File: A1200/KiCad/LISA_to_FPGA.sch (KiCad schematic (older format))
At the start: 30 parts, among them J1 Conn_01x01, J2 Conn_01x40, U1 LM1117-3.3, U2 74LVC162244ADGG, U3 74LVC162244ADGG, U4 LISA, U5 RP2354B

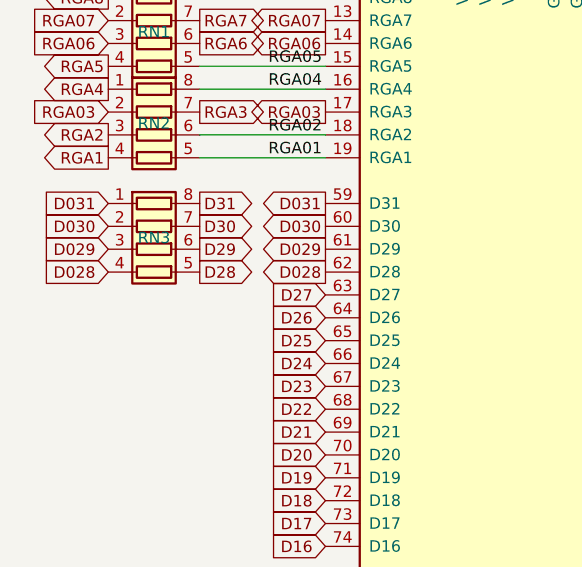
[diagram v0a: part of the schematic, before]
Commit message: Add RN4 resistor pack and route D27-D24
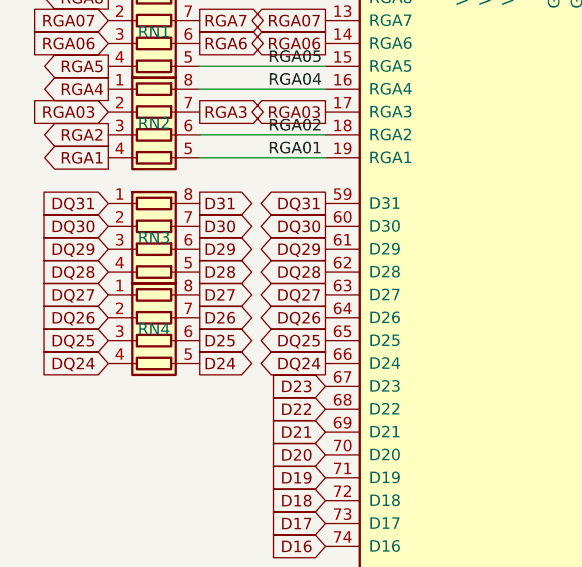
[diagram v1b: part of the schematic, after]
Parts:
- added RN4: R_Pack04, Resistor_SMD:R_Array_Convex_4x0603, symbol Device:R_Pack04
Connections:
- net D24: now also RN4.5 (R4.2); no longer U4.66 (D24)
- net D25: now also RN4.6 (R3.2); no longer U4.65 (D25)
- net D26: now also RN4.7 (R2.2); no longer U4.64 (D26)
- net D27: now also RN4.8 (R1.2); no longer U4.63 (D27)
- net D028 renamed DQ28
- net D029 renamed DQ29
- net D030 renamed DQ30
- net D031 renamed DQ31
- new net DQ24: RN4.4 (R4.1), U4.66 (D24)
- new net DQ25: RN4.3 (R3.1), U4.65 (D25)
- new net DQ26: RN4.2 (R2.1), U4.64 (D26)
- new net DQ27: RN4.1 (R1.1), U4.63 (D27)
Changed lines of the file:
@@
 Text GLabel 1150 2550 2    50   Output ~ 0
 D28
-Text GLabel 1700 2650 0    50   Input ~ 0
-D27
-Text GLabel 1700 2750 0    50   Input ~ 0
-D26
-Text GLabel 1700 2850 0    50   Input ~ 0
-D25
-Text GLabel 1700 2950 0    50   Input ~ 0
-D24
+Text GLabel 1700 2750 0    50   Output ~ 0
+DQ26
+Text GLabel 1700 2850 0    50   Output ~ 0
+DQ25
+Text GLabel 1700 2950 0    50   Output ~ 0
+DQ24
 Text GLabel 1700 3050 0    50   Input ~ 0
 D23
@@
 	1700 2050 1150 2050
 Text GLabel 1700 2250 0    50   Output ~ 0
-D031
+DQ31
 Text GLabel 1700 2350 0    50   Output ~ 0
-D030
+DQ30
 Text GLabel 1700 2450 0    50   Output ~ 0
-D029
+DQ29
 Text GLabel 1700 2550 0    50   Output ~ 0
-D028
+DQ28
 Text GLabel 750  2250 0    50   Input ~ 0
-D031
+DQ31
 Text GLabel 750  2350 0    50   Input ~ 0
-D030
+DQ30
 Text GLabel 750  2450 0    50   Input ~ 0
-D029
+DQ29
 Text GLabel 750  2550 0    50   Input ~ 0
-D028
+DQ28
+$Comp
+L Device:R_Pack04 RN4
+U 1 1 6AE6E351
+P 950 2850
+F 0 "RN4" V 900 2850 50  0000 C CNN
+F 1 "R_Pack04" V 950 2200 50  0001 C CNN
+F 2 "Resistor_SMD:R_Array_Convex_4x0603" V 1225 2850 50  0001 C CNN
+F 3 "~" H 950 2850 50  0001 C CNN
+	1    950  2850
+	0    1    1    0
+$EndComp
+Text GLabel 1700 2650 0    50   Output ~ 0
+DQ27
+Text GLabel 1150 2750 2    50   Output ~ 0
+D26
+Text GLabel 1150 2850 2    50   Output ~ 0
+D25
+Text GLabel 1150 2950 2    50   Output ~ 0
+D24
+Text GLabel 1150 2650 2    50   Output ~ 0
+D27
+Text GLabel 750  2650 0    50   Input ~ 0
+DQ27
+Text GLabel 750  2750 0    50   Input ~ 0
+DQ26
+Text GLabel 750  2850 0    50   Input ~ 0
+DQ25
+Text GLabel 750  2950 0    50   Input ~ 0
+DQ24
 $EndSCHEMATC

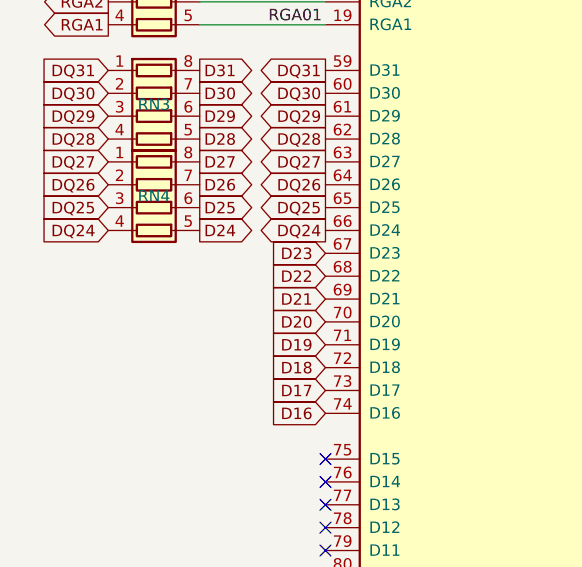
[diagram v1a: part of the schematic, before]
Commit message: Add RN5 resistor pack and route D23-D20
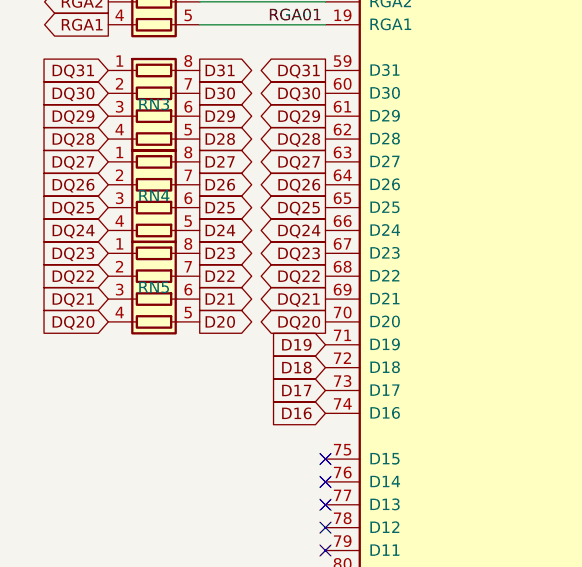
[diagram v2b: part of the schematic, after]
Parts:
- added RN5: R_Pack04, Resistor_SMD:R_Array_Convex_4x0603, symbol Device:R_Pack04
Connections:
- net D20: now also RN5.5 (R4.2); no longer U4.70 (D20)
- net D21: now also RN5.6 (R3.2); no longer U4.69 (D21)
- net D22: now also RN5.7 (R2.2); no longer U4.68 (D22)
- net D23: now also RN5.8 (R1.2); no longer U4.67 (D23)
- new net DQ20: RN5.4 (R4.1), U4.70 (D20)
- new net DQ21: RN5.3 (R3.1), U4.69 (D21)
- new net DQ22: RN5.2 (R2.1), U4.68 (D22)
- new net DQ23: RN5.1 (R1.1), U4.67 (D23)
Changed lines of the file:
@@
 Text GLabel 1700 2950 0    50   Output ~ 0
 DQ24
-Text GLabel 1700 3050 0    50   Input ~ 0
-D23
-Text GLabel 1700 3150 0    50   Input ~ 0
-D22
-Text GLabel 1700 3250 0    50   Input ~ 0
-D21
-Text GLabel 1700 3350 0    50   Input ~ 0
-D20
+Text GLabel 1700 3050 0    50   Output ~ 0
+DQ23
+Text GLabel 1700 3150 0    50   Output ~ 0
+DQ22
+Text GLabel 1700 3250 0    50   Output ~ 0
+DQ21
+Text GLabel 1700 3350 0    50   Output ~ 0
+DQ20
 Text GLabel 1700 3450 0    50   Input ~ 0
 D19
@@
 Text GLabel 750  2950 0    50   Input ~ 0
 DQ24
+$Comp
+L Device:R_Pack04 RN5
+U 1 1 6AEC9853
+P 950 3250
+F 0 "RN5" V 900 3250 50  0000 C CNN
+F 1 "R_Pack04" V 950 2600 50  0001 C CNN
+F 2 "Resistor_SMD:R_Array_Convex_4x0603" V 1225 3250 50  0001 C CNN
+F 3 "~" H 950 3250 50  0001 C CNN
+	1    950  3250
+	0    1    1    0
+$EndComp
+Text GLabel 750  3050 0    50   Input ~ 0
+DQ23
+Text GLabel 750  3150 0    50   Input ~ 0
+DQ22
+Text GLabel 750  3250 0    50   Input ~ 0
+DQ21
+Text GLabel 750  3350 0    50   Input ~ 0
+DQ20
+Text GLabel 1150 3050 2    50   Output ~ 0
+D23
+Text GLabel 1150 3150 2    50   Output ~ 0
+D22
+Text GLabel 1150 3250 2    50   Output ~ 0
+D21
+Text GLabel 1150 3350 2    50   Output ~ 0
+D20
 $EndSCHEMATC

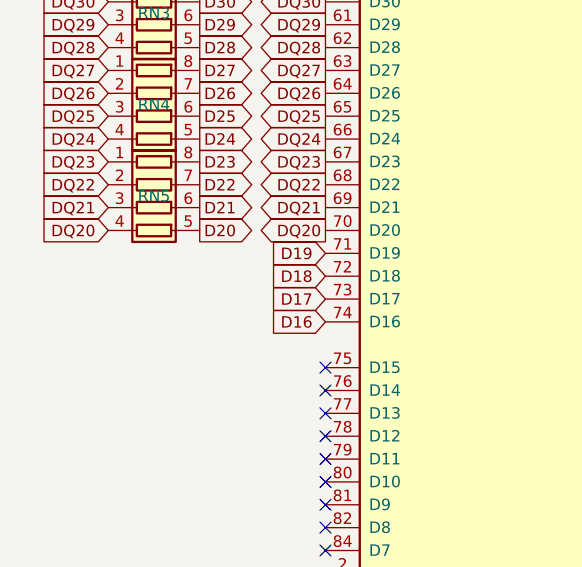
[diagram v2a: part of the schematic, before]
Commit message: Add RN6 resistor pack and route D19-D16, and some silkscreen fixes
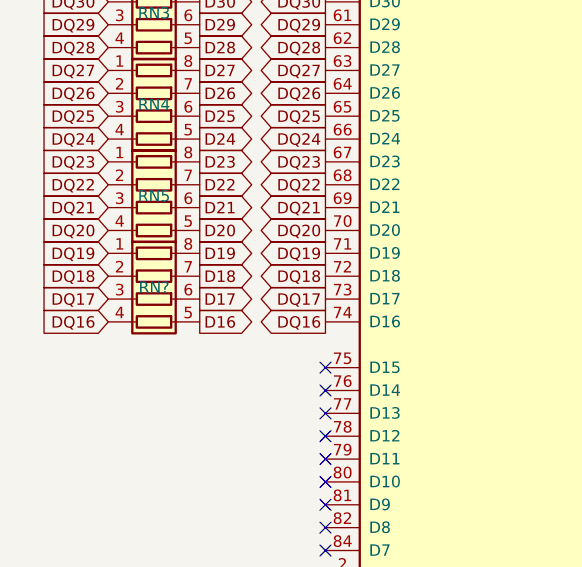
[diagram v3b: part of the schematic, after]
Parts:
- added RN?: R_Pack04, Resistor_SMD:R_Array_Convex_4x0603, symbol Device:R_Pack04
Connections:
- net D16: now also RN?.5 (R4.2); no longer U4.74 (D16)
- net D17: now also RN?.6 (R3.2); no longer U4.73 (D17)
- net D18: now also RN?.7 (R2.2); no longer U4.72 (D18)
- net D19: now also RN?.8 (R1.2); no longer U4.71 (D19)
- new net DQ16: RN?.4 (R4.1), U4.74 (D16)
- new net DQ17: RN?.3 (R3.1), U4.73 (D17)
- new net DQ18: RN?.2 (R2.1), U4.72 (D18)
- new net DQ19: RN?.1 (R1.1), U4.71 (D19)
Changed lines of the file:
@@
 Text GLabel 1700 3350 0    50   Output ~ 0
 DQ20
-Text GLabel 1700 3450 0    50   Input ~ 0
-D19
-Text GLabel 1700 3550 0    50   Input ~ 0
-D18
-Text GLabel 1700 3650 0    50   Input ~ 0
-D17
-Text GLabel 1700 3750 0    50   Input ~ 0
-D16
+Text GLabel 1700 3450 0    50   Output ~ 0
+DQ19
+Text GLabel 1700 3550 0    50   Output ~ 0
+DQ18
+Text GLabel 1700 3650 0    50   Output ~ 0
+DQ17
+Text GLabel 1700 3750 0    50   Output ~ 0
+DQ16
 Text GLabel 8200 4300 2    50   Input ~ 0
 RGA1
@@
 Text GLabel 1150 3350 2    50   Output ~ 0
 D20
+$Comp
+L Device:R_Pack04 RN?
+U 1 1 6AFA09CC
+P 950 3650
+F 0 "RN?" V 900 3650 50  0000 C CNN
+F 1 "R_Pack04" V 950 3000 50  0001 C CNN
+F 2 "Resistor_SMD:R_Array_Convex_4x0603" V 1225 3650 50  0001 C CNN
+F 3 "~" H 950 3650 50  0001 C CNN
+	1    950  3650
+	0    1    1    0
+$EndComp
+Text GLabel 1150 3450 2    50   Output ~ 0
+D19
+Text GLabel 1150 3550 2    50   Output ~ 0
+D18
+Text GLabel 1150 3650 2    50   Output ~ 0
+D17
+Text GLabel 1150 3750 2    50   Output ~ 0
+D16
+Text GLabel 750  3450 0    50   Input ~ 0
+DQ19
+Text GLabel 750  3550 0    50   Input ~ 0
+DQ18
+Text GLabel 750  3650 0    50   Input ~ 0
+DQ17
+Text GLabel 750  3750 0    50   Input ~ 0
+DQ16
 $EndSCHEMATC

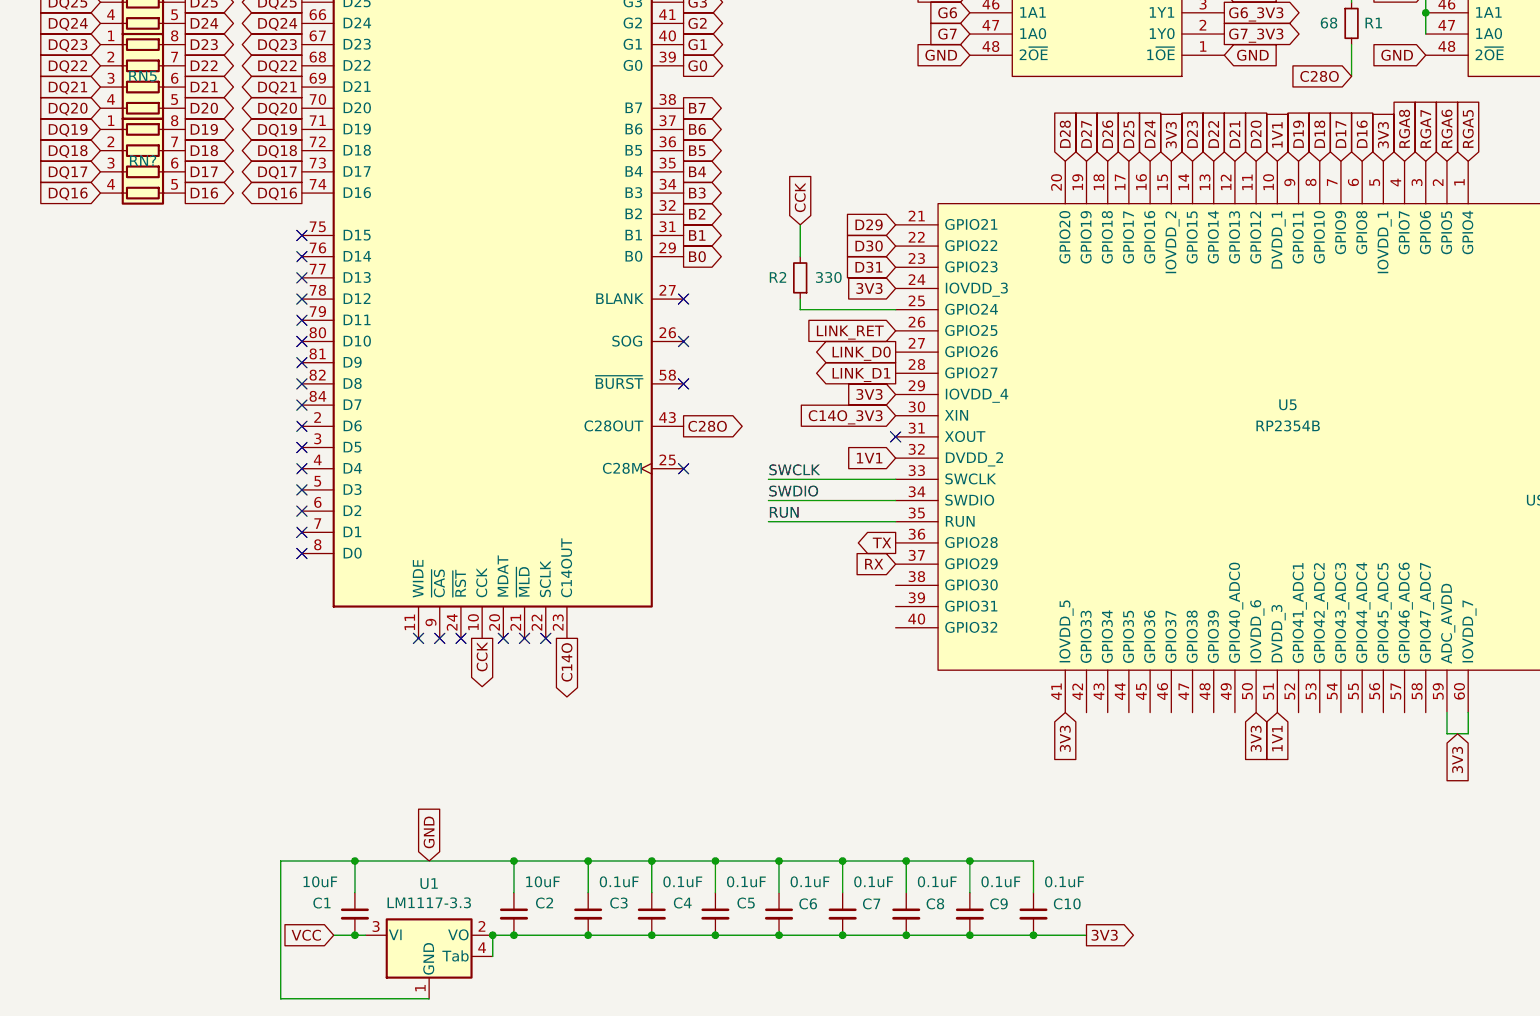
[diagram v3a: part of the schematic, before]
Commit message: Add decoupling caps for pin 5 and 15 on QFN-80 footprint, fixes of silkscreen on underside of board
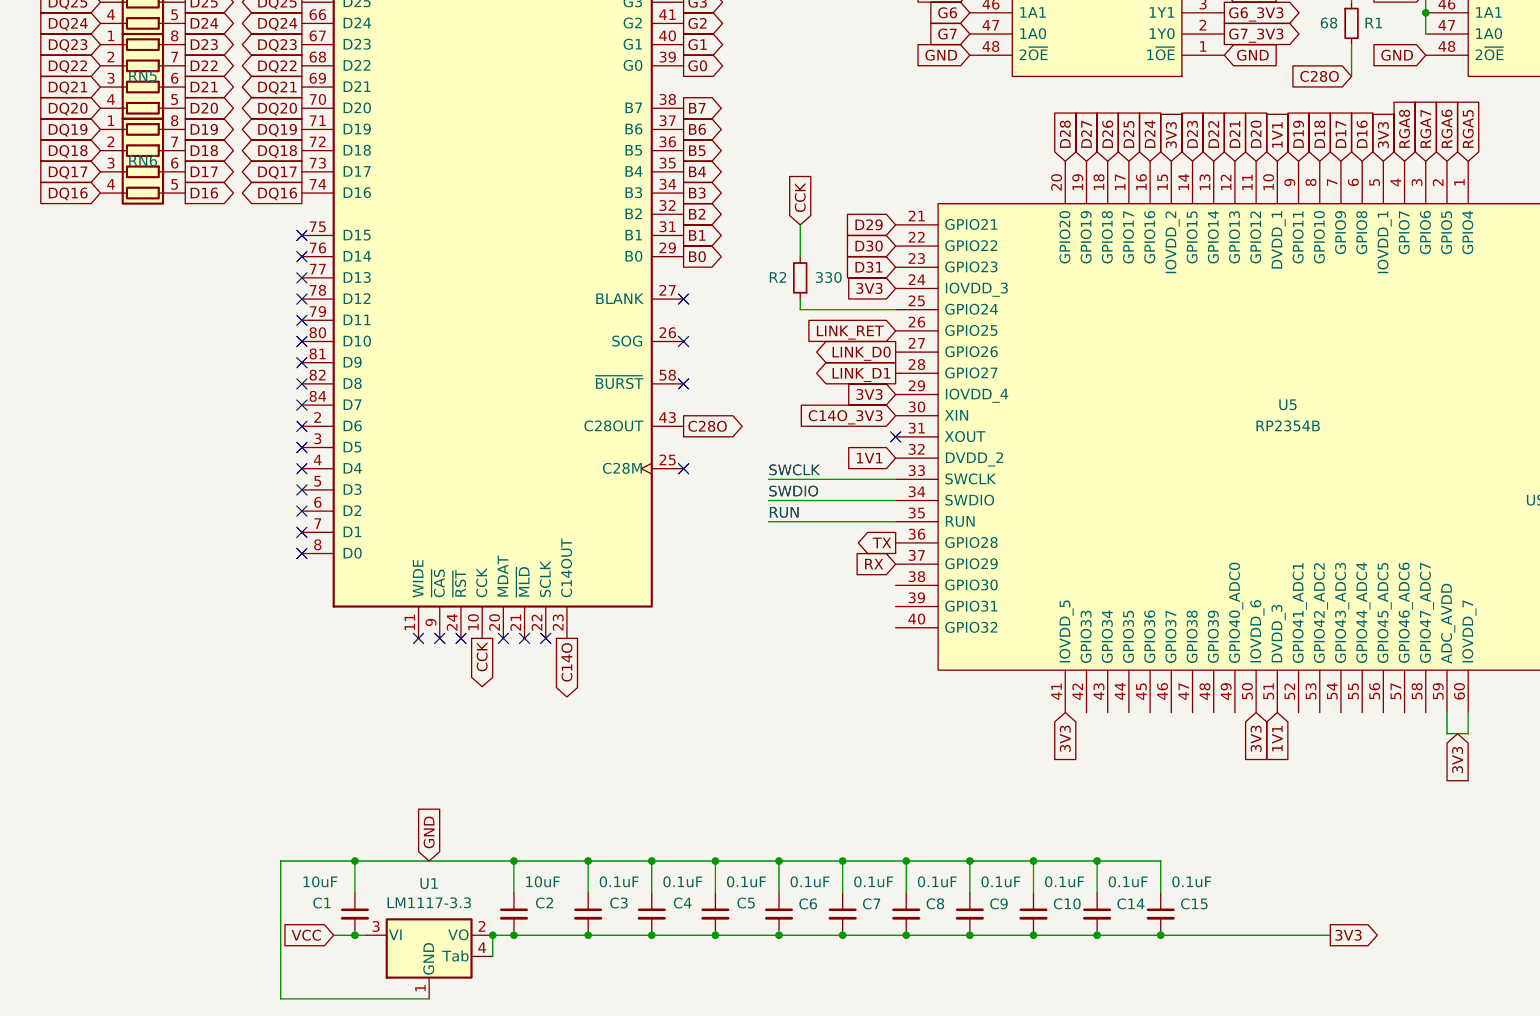
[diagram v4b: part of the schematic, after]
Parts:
- added C14, C15: 0.1uF, Capacitor_SMD:C_0603_1608Metric_Pad1.08x0.95mm_HandSolder, symbol Device:C_Small
- gave numbers to parts that had none: 1
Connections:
- net 3V3: now also C14.2, C15.2
- net GND: now also C14.1, C15.1
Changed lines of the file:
@@
 R5
 Connection ~ 5150 7250
-Wire Wire Line
-	5400 7250 5150 7250
 Connection ~ 4850 7250
 Wire Wire Line
@@
 	1    0    0    -1
 $EndComp
-Text GLabel 5400 7250 2    50   Output ~ 0
+Text GLabel 6550 7250 2    50   Output ~ 0
 3V3
 Connection ~ 2600 7250
@@
 D20
 $Comp
-L Device:R_Pack04 RN?
+L Device:R_Pack04 RN6
 U 1 1 6AFA09CC
 P 950 3650
-F 0 "RN?" V 900 3650 50  0000 C CNN
+F 0 "RN6" V 900 3650 50  0000 C CNN
 F 1 "R_Pack04" V 950 3000 50  0001 C CNN
 F 2 "Resistor_SMD:R_Array_Convex_4x0603" V 1225 3650 50  0001 C CNN
@@
 Text GLabel 750  3750 0    50   Input ~ 0
 DQ16
+$Comp
+L Device:C_Small C14
+U 1 1 6AFE1386
+P 5450 7150
+F 0 "C14" H 5542 7196 50  0000 L CNN
+F 1 "0.1uF" H 5500 7300 50  0000 L CNN
+F 2 "Capacitor_SMD:C_0603_1608Metric_Pad1.08x0.95mm_HandSolder" H 5450 7150 50  0001 C CNN
+F 3 "~" H 5450 7150 50  0001 C CNN
+	1    5450 7150
+	1    0    0    -1
+$EndComp
+Wire Wire Line
+	5450 7050 5450 6900
+Wire Wire Line
+	5450 6900 5150 6900
+Connection ~ 5150 6900
+Wire Wire Line
+	5150 7250 5450 7250
+Wire Wire Line
+	6550 7250 5750 7250
+Connection ~ 5450 7250
+$Comp
+L Device:C_Small C15
+U 1 1 6AFF9749
+P 5750 7150
+F 0 "C15" H 5842 7196 50  0000 L CNN
+F 1 "0.1uF" H 5800 7300 50  0000 L CNN
+F 2 "Capacitor_SMD:C_0603_1608Metric_Pad1.08x0.95mm_HandSolder" H 5750 7150 50  0001 C CNN
+F 3 "~" H 5750 7150 50  0001 C CNN
+	1    5750 7150
+	1    0    0    -1
+$EndComp
+Connection ~ 5750 7250
+Wire Wire Line
+	5750 7250 5450 7250
+Wire Wire Line
+	5750 7050 5750 6900
+Wire Wire Line
+	5750 6900 5450 6900
+Connection ~ 5450 6900
 $EndSCHEMATC

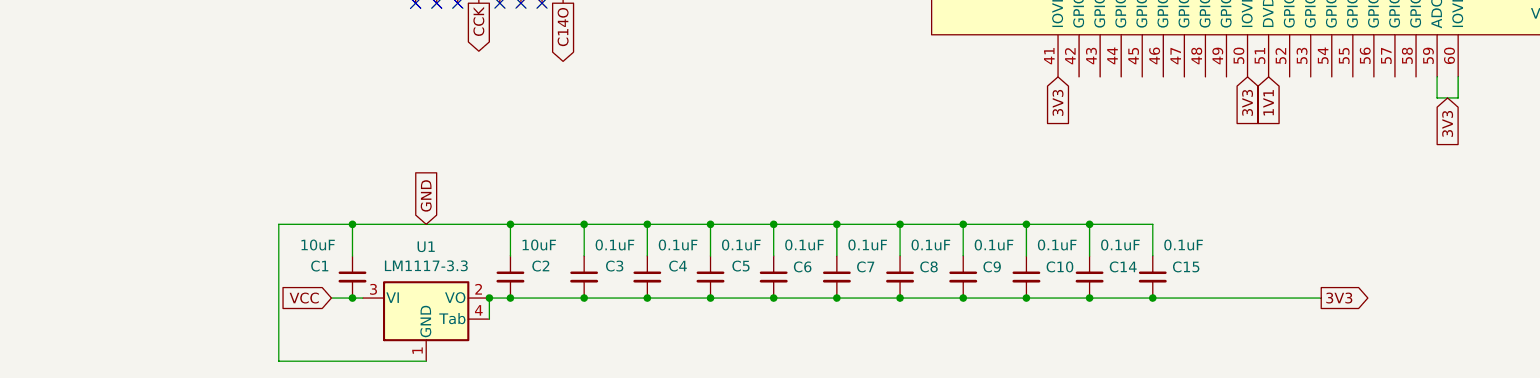
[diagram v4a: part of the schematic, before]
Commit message: Add decoupling cap for pin 76 on QFN-80 footprint
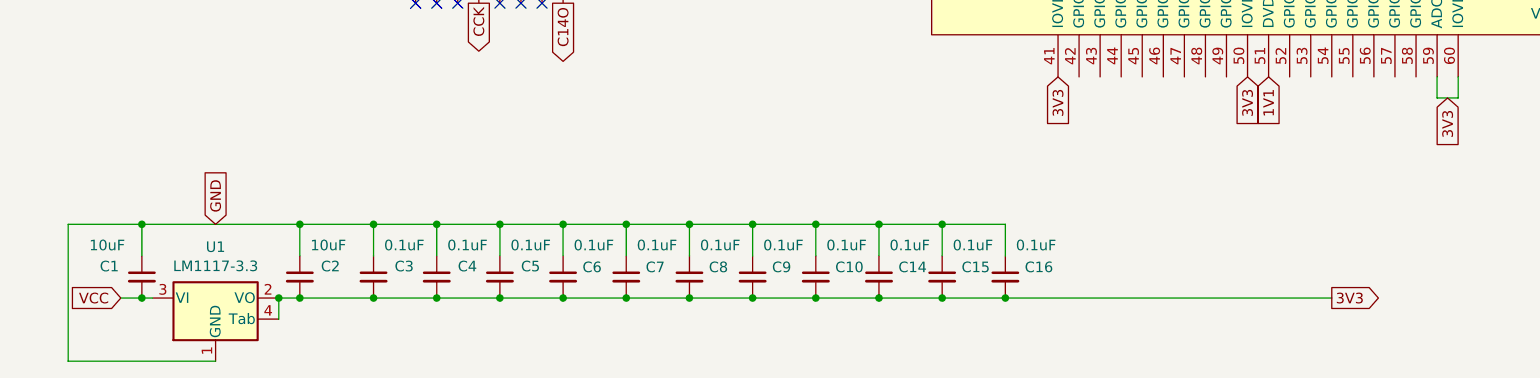
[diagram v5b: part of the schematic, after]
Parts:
- added C16: 0.1uF, Capacitor_SMD:C_0603_1608Metric_Pad1.08x0.95mm_HandSolder, symbol Device:C_Small
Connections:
- net 3V3: now also C16.2
- net GND: now also C16.1
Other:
- moved on the sheet: C1, C10, C14, C15, C2, C3, C4, C5, C6, C7, C8, C9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

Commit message: Add decoupling cap for pin 24 on QFN-80 footprint
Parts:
- added C17: 0.1uF, Capacitor_SMD:C_0603_1608Metric_Pad1.08x0.95mm_HandSolder, symbol Device:C_Small
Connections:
- net 3V3: now also C17.2
- net GND: now also C17.1
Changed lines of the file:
@@
 Connection ~ 5050 7250
 Wire Wire Line
-	5050 7250 6600 7250
+	5050 7250 5350 7250
 Wire Wire Line
 	5050 7050 5050 6900
@@
 	5050 6900 4750 6900
 Connection ~ 4750 6900
+$Comp
+L Device:C_Small C17
+U 1 1 6B057B5C
+P 5350 7150
+F 0 "C17" H 5442 7196 50  0000 L CNN
+F 1 "0.1uF" H 5400 7300 50  0000 L CNN
+F 2 "Capacitor_SMD:C_0603_1608Metric_Pad1.08x0.95mm_HandSolder" H 5350 7150 50  0001 C CNN
+F 3 "~" H 5350 7150 50  0001 C CNN
+	1    5350 7150
+	1    0    0    -1
+$EndComp
+Connection ~ 5350 7250
+Wire Wire Line
+	5350 7250 6600 7250
+Wire Wire Line
+	5350 7050 5350 6900
+Wire Wire Line
+	5350 6900 5050 6900
+Connection ~ 5050 6900
 $EndSCHEMATC
